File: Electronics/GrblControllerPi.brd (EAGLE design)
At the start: 85.1 x 56.1 mm, 21 parts, among them IC1 ATMEGA168-20P, SW1 SPST_TACT-EVQQ2

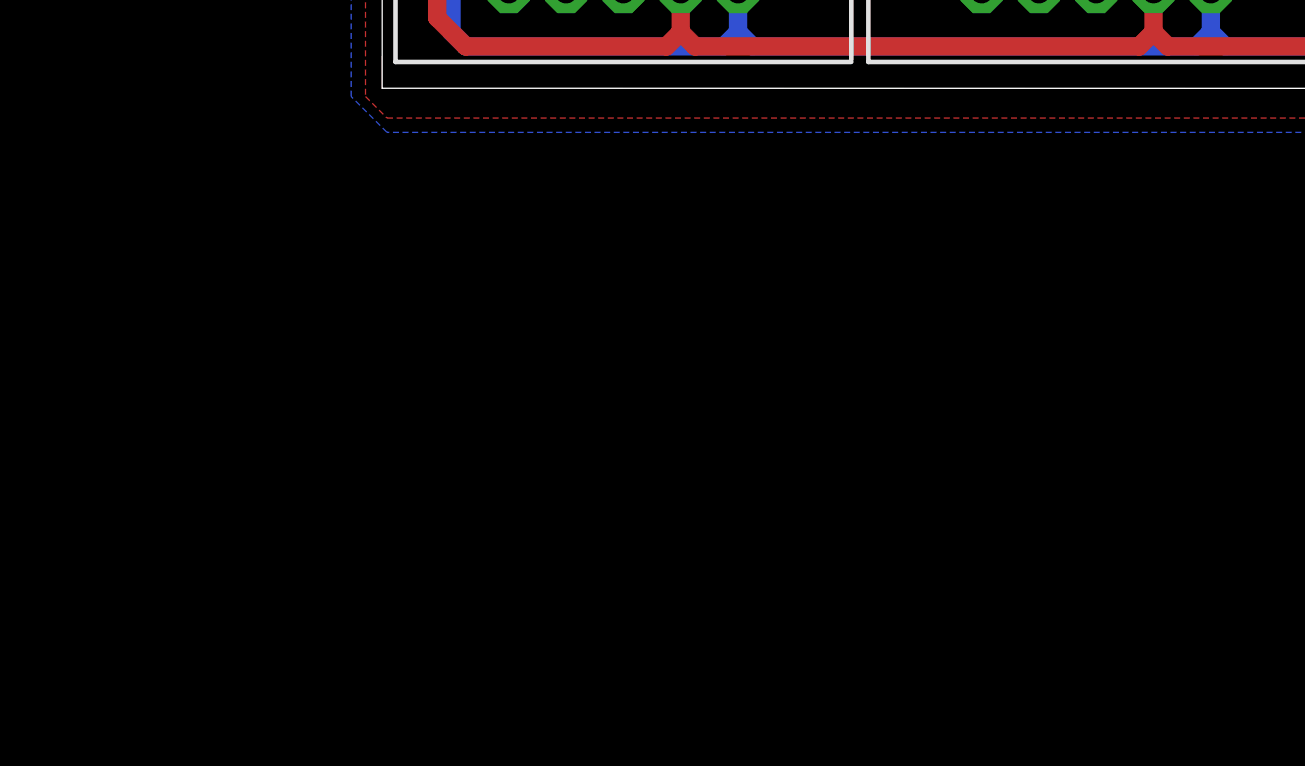
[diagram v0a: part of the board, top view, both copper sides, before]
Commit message: Added Stepper Driver
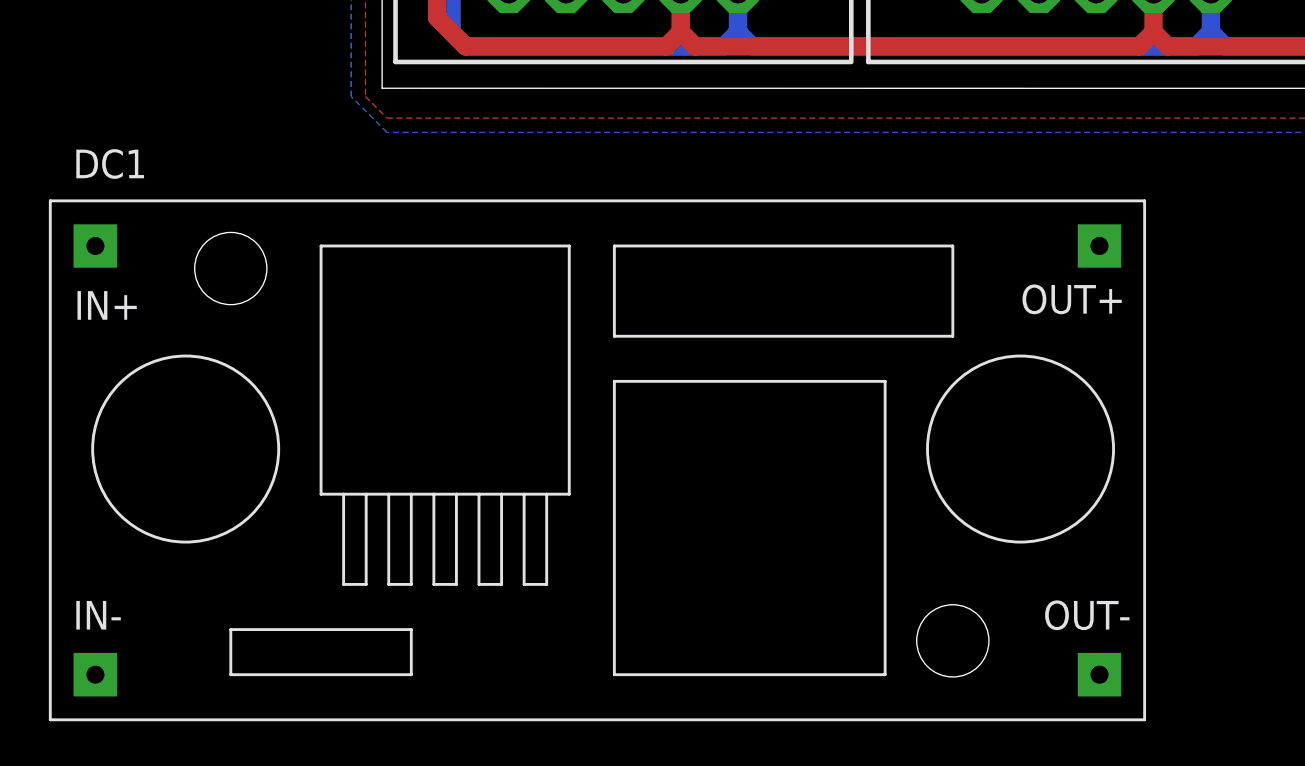
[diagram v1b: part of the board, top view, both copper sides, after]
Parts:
- added DC1: (no value), OpenHardware.co.za:BUCKBOOST
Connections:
- new net IN+: DC1.IN+
- new net OUT+: DC1.OU+
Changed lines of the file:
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@@
 <layers>
 <layer number="1" name="Top" color="4" fill="1" visible="yes" active="yes"/>
+<layer number="2" name="Route2" color="1" fill="3" visible="no" active="yes"/>
+<layer number="3" name="Route3" color="4" fill="3" visible="no" active="yes"/>
+<layer number="4" name="Route4" color="1" fill="4" visible="no" active="yes"/>
+<layer number="5" name="Route5" color="4" fill="4" visible="no" active="yes"/>
+<layer number="6" name="Route6" color="1" fill="8" visible="no" active="yes"/>
+<layer number="7" name="Route7" color="4" fill="8" visible="no" active="yes"/>
+<layer number="8" name="Route8" color="1" fill="2" visible="no" active="yes"/>
+<layer number="9" name="Route9" color="4" fill="2" visible="no" active="yes"/>
+<layer number="10" name="Route10" color="1" fill="7" visible="no" active="yes"/>
+<layer number="11" name="Route11" color="4" fill="7" visible="no" active="yes"/>
+<layer number="12" name="Route12" color="1" fill="5" visible="no" active="yes"/>
+<layer number="13" name="Route13" color="4" fill="5" visible="no" active="yes"/>
+<layer number="14" name="Route14" color="1" fill="6" visible="no" active="yes"/>
+<layer number="15" name="Route15" color="4" fill="6" visible="no" active="yes"/>
 <layer number="16" name="Bottom" color="1" fill="1" visible="yes" active="yes"/>
 <layer number="17" name="Pads" color="2" fill="1" visible="yes" active="yes"/>
@@
 <element name="R4" library="dp_devices" package="R1206" value="1K" x="38.4175" y="18.415" rot="R180"/>
 <element name="LED1" library="adafruit" package="CHIPLED_1206" value="" x="38.4175" y="23.495" rot="R90"/>
+<element name="DC1" library="OpenHardware.co.za" package="BUCKBOOST" value="" x="-14.605" y="-27.94"/>
 </elements>
 <signals>
@@
 <via x="19.05" y="16.1925" extent="1-16" drill="0.6" shape="square"/>
 </signal>
+<signal name="IN+">
+<contactref element="DC1" pad="IN+"/>
+</signal>
+<signal name="OUT+">
+<contactref element="DC1" pad="OU+"/>
+</signal>
 </signals>

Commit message: Minor Tweaks to hardware + Added GrblpiB+ boards
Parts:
- removed DC1: (no value), OpenHardware.co.za:BUCKBOOST
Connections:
- removed net IN+: DC1.IN+
- removed net OUT+: DC1.OU+
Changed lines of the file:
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@@
 <element name="R4" library="dp_devices" package="R1206" value="1K" x="38.4175" y="18.415" rot="R180"/>
 <element name="LED1" library="adafruit" package="CHIPLED_1206" value="" x="38.4175" y="23.495" rot="R90"/>
-<element name="DC1" library="OpenHardware.co.za" package="BUCKBOOST" value="" x="-14.605" y="-27.94"/>
 </elements>
 <signals>
@@
 <via x="19.05" y="16.1925" extent="1-16" drill="0.6" shape="square"/>
 </signal>
-<signal name="IN+">
-<contactref element="DC1" pad="IN+"/>
-</signal>
-<signal name="OUT+">
-<contactref element="DC1" pad="OU+"/>
-</signal>
 </signals>
